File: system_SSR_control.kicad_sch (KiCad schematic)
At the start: 13 parts, among them Q1 2.1V, Q2 2N7000, Q3 2N7000, SW1 FSM2JSMA, SW2 FSM2JSMA

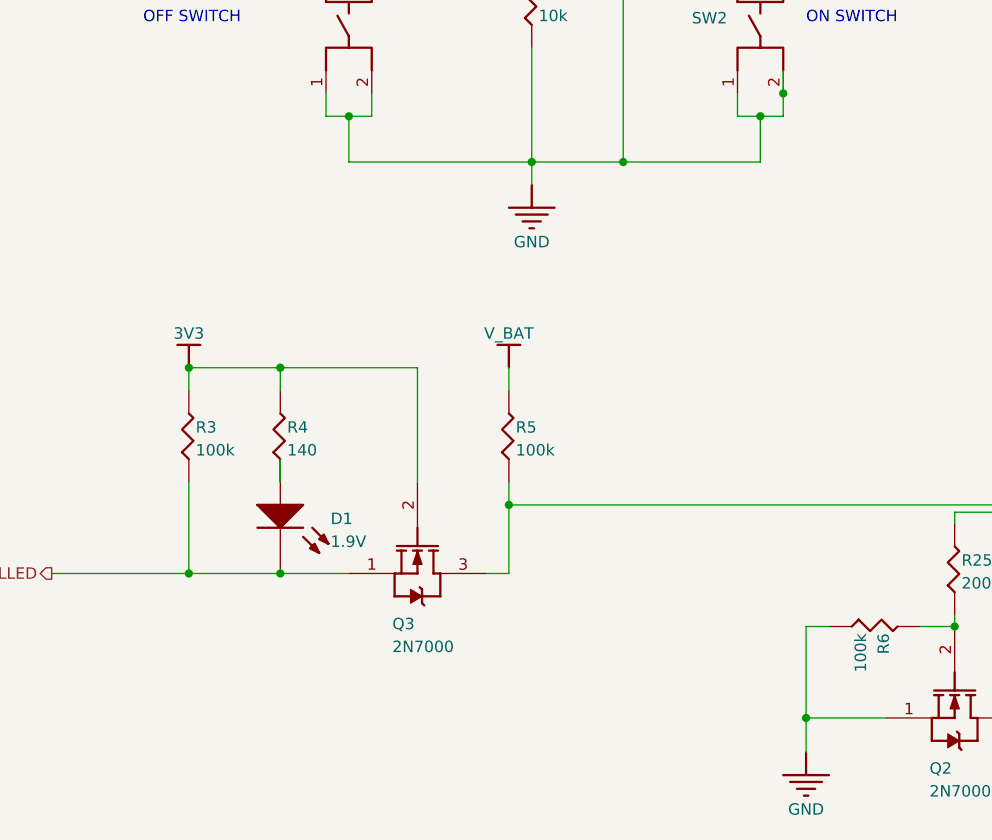
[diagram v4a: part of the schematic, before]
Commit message: updated power and ground symbols in schematic to kicad library version
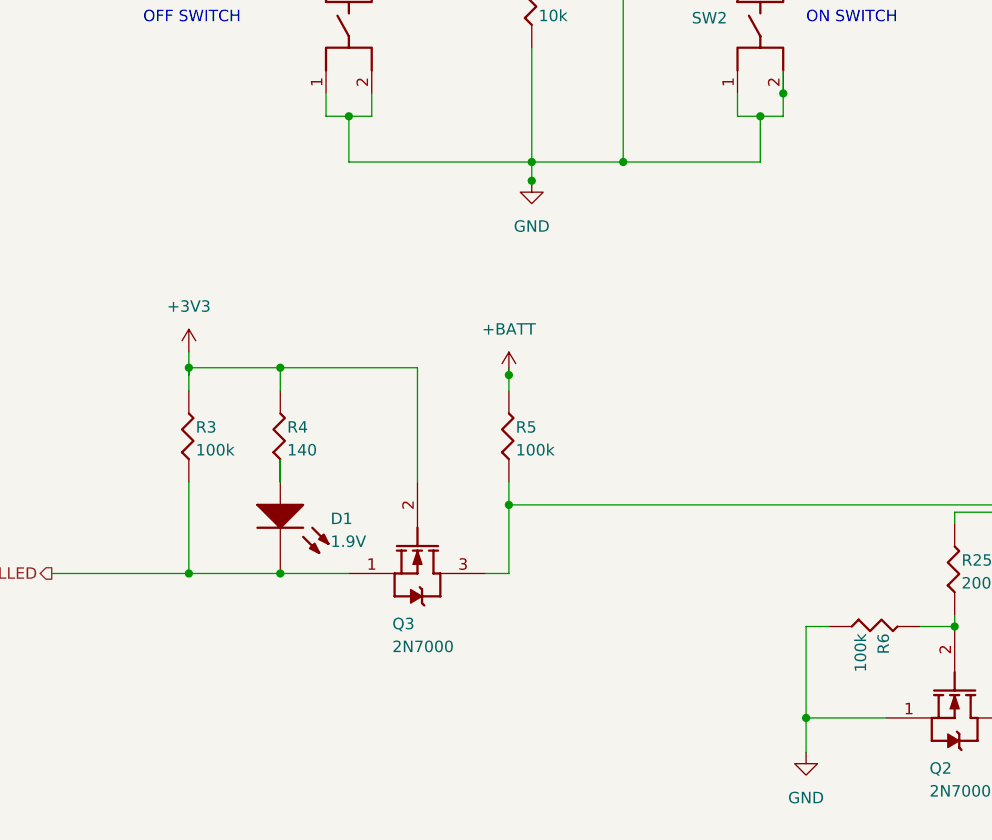
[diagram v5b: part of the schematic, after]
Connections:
- net 3V3 renamed +3V3
- net V_BAT renamed +BATT
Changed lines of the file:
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@@
   (junction (at 119.38 86.36) (diameter 0) (color 0 0 0 0)
   )
+  (junction (at 139.7 118.11) (diameter 0) (color 0 0 0 0)
+  )
+  (junction (at 165.1 110.9472) (diameter 0) (color 0 0 0 0)
+  )
+  (junction (at 101.6 161.7472) (diameter 0) (color 0 0 0 0)
+  )
   (junction (at 101.6 138.8872) (diameter 0) (color 0 0 0 0)
   )
-  (junction (at 165.1 110.9472) (diameter 0) (color 0 0 0 0)
-  )
-  (junction (at 101.6 161.7472) (diameter 0) (color 0 0 0 0)
+  (junction (at 137.16 139.7) (diameter 0) (color 0 0 0 0)
   )
   (junction (at 165.1 83.82) (diameter 0) (color 0 0 0 0)
@@
     (stroke (width 0) (type default))
   )
+  (wire (pts (xy 101.6 137.16) (xy 101.6 138.8872))
+    (stroke (width 0) (type default))
+  )
   (wire (pts (xy 111.76 161.7472) (xy 119.38 161.7472))
     (stroke (width 0.254) (type default))
@@
     (stroke (width 0.254) (type default))
   )
+  (wire (pts (xy 139.7 118.11) (xy 139.7 118.5672))
+    (stroke (width 0.254) (type default))
+  )
   (wire (pts (xy 165.1 90.6272) (xy 165.1 83.82))
     (stroke (width 0.254) (type default))
   )
-  (wire (pts (xy 139.7 116.0272) (xy 139.7 118.5672))
+  (wire (pts (xy 139.7 116.0272) (xy 139.7 118.11))
     (stroke (width 0.254) (type default))
   )
@@
   (wire (pts (xy 101.6 161.7472) (xy 111.76 161.7472))
     (stroke (width 0.254) (type default))
+  )
+  (wire (pts (xy 101.6 138.8872) (xy 101.6 139.7))
+    (stroke (width 0) (type default))
   )
   (wire (pts (xy 127 138.8872) (xy 111.76 138.8872))
@@
     (stroke (width 0.254) (type default))
   )
-  (wire (pts (xy 137.16 138.8872) (xy 137.16 141.4272))
+  (wire (pts (xy 137.16 138.8872) (xy 137.16 139.7))
     (stroke (width 0.254) (type default))
   )
@@
   )
   (wire (pts (xy 116.84 110.9472) (xy 119.38 110.9472))
+    (stroke (width 0.254) (type default))
+  )
+  (wire (pts (xy 137.16 139.7) (xy 137.16 141.4272))
     (stroke (width 0.254) (type default))
   )
@@
     (effects (font (size 1.27 1.27)) (justify left))
   )
-  (symbol (lib_id "MEB-altium-import:GND") (at 170.18 181.61 0) (unit 1)
-    (in_bom yes) (on_board yes) (dnp no)
-    (property "Reference" "#PWR0123" (at 170.18 181.61 0)
-      (effects (font (size 1.27 1.27)) hide)
-    )
-    (property "Value" "GND" (at 170.18 187.96 0)
-      (effects (font (size 1.27 1.27)))
-    )
-    (property "Footprint" "" (at 170.18 181.61 0)
-      (effects (font (size 1.27 1.27)) hide)
-    )
-    (property "Datasheet" "" (at 170.18 181.61 0)
-      (effects (font (size 1.27 1.27)) hide)
-    )
-    (pin "")
-    (instances
-      (project "MEB"
-        (path "/228e4997-23c1-4c21-939b-583cad26a5e3/d2748488-1aa2-4890-bfa9-60c09f864312"
-          (reference "#PWR0123") (unit 1)
-        )
-      )
-    )
-  )
-  (symbol (lib_id "MEB-altium-import:3V3") (at 101.6 138.8872 180) (unit 1)
-    (in_bom yes) (on_board yes) (dnp no)
-    (property "Reference" "#PWR0124" (at 101.6 138.8872 0)
-      (effects (font (size 1.27 1.27)) hide)
-    )
-    (property "Value" "3V3" (at 101.6 135.0772 0)
-      (effects (font (size 1.27 1.27)))
-    )
-    (property "Footprint" "" (at 101.6 138.8872 0)
-      (effects (font (size 1.27 1.27)) hide)
-    )
-    (property "Datasheet" "" (at 101.6 138.8872 0)
-      (effects (font (size 1.27 1.27)) hide)
-    )
-    (pin "")
-    (instances
-      (project "MEB"
-        (path "/228e4997-23c1-4c21-939b-583cad26a5e3/d2748488-1aa2-4890-bfa9-60c09f864312"
-          (reference "#PWR0124") (unit 1)
-        )
-      )
-    )
-  )
   (symbol (lib_id "MEB-altium-import:system_SSR_control_1_ERJ-6ENF1002V") (at 139.7 98.2472 0) (unit 1)
     (in_bom yes) (on_board yes) (dnp no)
@@
     )
   )
-  (symbol (lib_id "MEB-altium-import:GND") (at 139.7 118.5672 0) (unit 1)
-    (in_bom yes) (on_board yes) (dnp no)
-    (property "Reference" "#PWR0122" (at 139.7 118.5672 0)
-      (effects (font (size 1.27 1.27)) hide)
-    )
-    (property "Value" "GND" (at 139.7 124.9172 0)
-      (effects (font (size 1.27 1.27)))
-    )
-    (property "Footprint" "" (at 139.7 118.5672 0)
-      (effects (font (size 1.27 1.27)) hide)
-    )
-    (property "Datasheet" "" (at 139.7 118.5672 0)
-      (effects (font (size 1.27 1.27)) hide)
-    )
-    (pin "")
-    (instances
-      (project "MEB"
-        (path "/228e4997-23c1-4c21-939b-583cad26a5e3/d2748488-1aa2-4890-bfa9-60c09f864312"
-          (reference "#PWR0122") (unit 1)
-        )
-      )
-    )
-  )
   (symbol (lib_id "MEB-altium-import:system_SSR_control_3_WE-LED_K1A2-2") (at 111.76 154.1272 0) (unit 1)
     (in_bom yes) (on_board yes) (dnp no)
@@
     )
   )
+  (symbol (lib_id "power:GND") (at 139.7 118.11 0) (unit 1)
+    (in_bom yes) (on_board yes) (dnp no) (fields_autoplaced)
+    (property "Reference" "#PWR030" (at 139.7 124.46 0)
+      (effects (font (size 1.27 1.27)) hide)
+    )
+    (property "Value" "GND" (at 139.7 123.19 0)
+      (effects (font (size 1.27 1.27)))
+    )
+    (property "Footprint" "" (at 139.7 118.11 0)
+      (effects (font (size 1.27 1.27)) hide)
+    )
+    (property "Datasheet" "" (at 139.7 118.11 0)
+      (effects (font (size 1.27 1.27)) hide)
+    )
+    (pin "1")
+    (instances
+      (project "MEB"
+        (path "/228e4997-23c1-4c21-939b-583cad26a5e3/3aab6a70-cc66-4393-a750-92acad576aaa"
+          (reference "#PWR030") (unit 1)
+        )
+        (path "/228e4997-23c1-4c21-939b-583cad26a5e3/d2748488-1aa2-4890-bfa9-60c09f864312"
+          (reference "#PWR032") (unit 1)
+        )
+      )
+    )
+  )
   (symbol (lib_id "MEB-altium-import:system_SSR_control_1_FSM2JSMA") (at 165.1 100.7872 0) (unit 1)
     (in_bom yes) (on_board yes) (dnp no)
@@
     )
   )
-  (symbol (lib_id "MEB-altium-import:V_BAT") (at 137.16 138.8872 180) (unit 1)
-    (in_bom yes) (on_board yes) (dnp no)
-    (property "Reference" "#PWR0125" (at 137.16 138.8872 0)
-      (effects (font (size 1.27 1.27)) hide)
-    )
-    (property "Value" "V_BAT" (at 137.16 135.0772 0)
+  (symbol (lib_id "power:GND") (at 170.18 181.61 0) (unit 1)
+    (in_bom yes) (on_board yes) (dnp no) (fields_autoplaced)
+    (property "Reference" "#PWR030" (at 170.18 187.96 0)
+      (effects (font (size 1.27 1.27)) hide)
+    )
+    (property "Value" "GND" (at 170.18 186.69 0)
       (effects (font (size 1.27 1.27)))
     )
-    (property "Footprint" "" (at 137.16 138.8872 0)
-      (effects (font (size 1.27 1.27)) hide)
-    )
-    (property "Datasheet" "" (at 137.16 138.8872 0)
-      (effects (font (size 1.27 1.27)) hide)
-    )
-    (pin "")
-    (instances
-      (project "MEB"
-        (path "/228e4997-23c1-4c21-939b-583cad26a5e3/d2748488-1aa2-4890-bfa9-60c09f864312"
-          (reference "#PWR0125") (unit 1)
+    (property "Footprint" "" (at 170.18 181.61 0)
+      (effects (font (size 1.27 1.27)) hide)
+    )
+    (property "Datasheet" "" (at 170.18 181.61 0)
+      (effects (font (size 1.27 1.27)) hide)
+    )
+    (pin "1")
+    (instances
+      (project "MEB"
+        (path "/228e4997-23c1-4c21-939b-583cad26a5e3/3aab6a70-cc66-4393-a750-92acad576aaa"
+          (reference "#PWR030") (unit 1)
+        )
+        (path "/228e4997-23c1-4c21-939b-583cad26a5e3/d2748488-1aa2-4890-bfa9-60c09f864312"
+          (reference "#PWR031") (unit 1)
+        )
+      )
+    )
+  )
+  (symbol (lib_id "power:+BATT") (at 137.16 139.7 0) (unit 1)
+    (in_bom yes) (on_board yes) (dnp no) (fields_autoplaced)
+    (property "Reference" "#PWR041" (at 137.16 143.51 0)
+      (effects (font (size 1.27 1.27)) hide)
+    )
+    (property "Value" "+BATT" (at 137.16 134.62 0)
+      (effects (font (size 1.27 1.27)))
+    )
+    (property "Footprint" "" (at 137.16 139.7 0)
+      (effects (font (size 1.27 1.27)) hide)
+    )
+    (property "Datasheet" "" (at 137.16 139.7 0)
+      (effects (font (size 1.27 1.27)) hide)
+    )
+    (pin "1")
+    (instances
+      (project "MEB"
+        (path "/228e4997-23c1-4c21-939b-583cad26a5e3"
+          (reference "#PWR041") (unit 1)
+        )
+        (path "/228e4997-23c1-4c21-939b-583cad26a5e3/d2748488-1aa2-4890-bfa9-60c09f864312"
+          (reference "#PWR042") (unit 1)
         )
       )
@@
         )
       )
+    )
+  )
+  (symbol (lib_id "power:+3V3") (at 101.6 137.16 0) (unit 1)
+    (in_bom yes) (on_board yes) (dnp no) (fields_autoplaced)
+    (property "Reference" "#PWR036" (at 101.6 140.97 0)
+      (effects (font (size 1.27 1.27)) hide)
+    )
+    (property "Value" "+3V3" (at 101.6 132.08 0)
+      (effects (font (size 1.27 1.27)))
+    )
+    (property "Footprint" "" (at 101.6 137.16 0)
+      (effects (font (size 1.27 1.27)) hide)
+    )
+    (property "Datasheet" "" (at 101.6 137.16 0)
+      (effects (font (size 1.27 1.27)) hide)
+    )
+    (pin "1")
+    (instances
+      (project "MEB"
+        (path "/228e4997-23c1-4c21-939b-583cad26a5e3"
+          (reference "#PWR036") (unit 1)
+        )
+        (path "/228e4997-23c1-4c21-939b-583cad26a5e3/d2748488-1aa2-4890-bfa9-60c09f864312"
+          (reference "#PWR039") (unit 1)
+        )
+      )

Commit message: no changes
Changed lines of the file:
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@@
-    (stroke (width 0.254) (type default))
-  )
-  (wire (pts (xy 186.69 154.94) (xy 186.69 156.21))
     (stroke (width 0.254) (type default))
   )
@@
     (stroke (width 0.254) (type default))
   )
-  (wire (pts (xy 186.69 154.94) (xy 222.25 154.94))
+  (wire (pts (xy 186.69 156.21) (xy 185.42 156.21))
     (stroke (width 0.254) (type default))
   )
@@
     (stroke (width 0.254) (type default))
   )
+  (wire (pts (xy 185.42 157.48) (xy 171.45 157.48))
+    (stroke (width 0.254) (type default))
+  )
   (wire (pts (xy 149.86 75.3872) (xy 149.86 77.9272))
     (stroke (width 0.254) (type default))
@@
   )
   (wire (pts (xy 149.86 116.0272) (xy 149.86 88.0872))
+    (stroke (width 0.254) (type default))
+  )
+  (wire (pts (xy 185.42 156.21) (xy 185.42 157.48))
     (stroke (width 0.254) (type default))
   )
@@
     (effects (font (size 1.27 1.27)) (justify left bottom))
   )
-  (label "SW_ARM" (at 198.12 154.94 0) (fields_autoplaced)
-    (effects (font (size 1.27 1.27)) (justify left bottom))
-  )
   (hierarchical_label "SYS_ON" (shape input) (at 185.42 83.82 0) (fields_autoplaced)
     (effects (font (size 1.27 1.27)) (justify left))
@@
     (effects (font (size 1.27 1.27)) (justify right))
   )
-  (hierarchical_label "SW_ARM" (shape input) (at 222.25 154.94 0) (fields_autoplaced)
-    (effects (font (size 1.27 1.27)) (justify left))
+  (hierarchical_label "SW_ARM" (shape input) (at 171.45 157.48 180) (fields_autoplaced)
+    (effects (font (size 1.27 1.27)) (justify right))
   )
   (symbol (lib_id "MEB-altium-import:system_SSR_control_1_ERJ-6ENF1002V") (at 139.7 98.2472 0) (unit 1)
